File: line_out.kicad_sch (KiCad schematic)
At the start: 0 parts

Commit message: updates
* add line out
* fix almost all erc
* some more random edits
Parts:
- added C154, C157: 10u, invendelirium_audio:C_0603, symbol Device:C
- added C155: 1u, invendelirium_audio:C_0603, symbol Device:C
- added C156: 100n, invendelirium_audio:C_0603, symbol Device:C
- added C158, C159, C160, C161: 5.6n, invendelirium_audio:C_0603, symbol Device:C
- added D19, D20: 5V, symbol Device:D_TVS
- added J8: AudioJack4, Connector_Audio:Jack_3.5mm_PJ320D_Horizontal, symbol Connector_Audio:AudioJack4
- added R223, R233, R237, R238: 560, invendelirium_audio:R_0603, symbol Device:R_Small
- added R224, R225, R231, R232: 20k, invendelirium_audio:R_0603, symbol Device:R_Small
- added R226, R229: 560?, invendelirium_audio:R_0603, symbol Device:R_Small
- added R227, R236: 1k, invendelirium_audio:R_0603, symbol Device:R_Small
- added R228, R230, R234, R235: 4.7k, invendelirium_audio:R_0603, symbol Device:R_Small
- added R239: 10, invendelirium_audio:R_0603, symbol Device:R_Small
- added U29: max97220, invendelirium_audio:qfn_4p4p_3x3mm, symbol invendelirium_audio:max97220
- added s32: lineout0, invendelirium_general:pad_1.2x1.5, symbol Connector:TestPoint
- added s33: lineout1, invendelirium_general:pad_1.2x1.5, symbol Connector:TestPoint
- added s34: lineout2, invendelirium_general:pad_1.2x1.5, symbol Connector:TestPoint
- added s35: lineout3, invendelirium_general:pad_1.2x1.5, symbol Connector:TestPoint
- added s36: ref, invendelirium_general:pad_1.2x1.5, symbol Connector:TestPoint
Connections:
- new net: D20.2 (A2), J8.R1, R232.2, R236.2, U29.10, s33.1
- new net: D19.2 (A2), J8.T, R224.2, R227.2, U29.12, s32.1
- new net: R226.2, R235.1
- new net: C154.1, R239.2, U29.1 (pvdd), U29.13 (svdd), U29.9 (svdd2)
- new net: R230.2, R231.1, U29.7 (+)
- new net: C159.1, R223.2, R228.1
- new net: C158.1, R233.2, R234.1
- new net: R225.1, R235.2, U29.15 (+)
- new net: R228.2, R232.1, U29.8 (-)
- new net: C157.1, U29.5 (pvss)
- new net: C161.1, R238.2, s35.1
- new net: C160.1, R237.2, s34.1
- new net: C155.1, U29.4 (c1n)
- new net: C155.2, U29.2 (c1p)
- new net: R224.1, R234.2, U29.14 (-)
- new net: R229.2, R230.1
- new net: C156.1, U29.11 (bias)
- new net 5V: R239.1
- new net GND: C154.2, C156.2, C157.2, C158.2, C159.2, C160.2, C161.2, D19.1 (A1), D20.1 (A1), J8.R2, J8.S, R225.2, R227.1, R231.2, R236.1, U29.3 (pgnd), U29.6 (sgnd)
- new net en: U29.16 (EN)
- new net input_ref: R226.1, R229.1, s36.1
- new net s0: R233.1
- new net s1: R223.1
- new net s2: R237.1
- new net s3: R238.1
- no-connect marks 0 -> 1

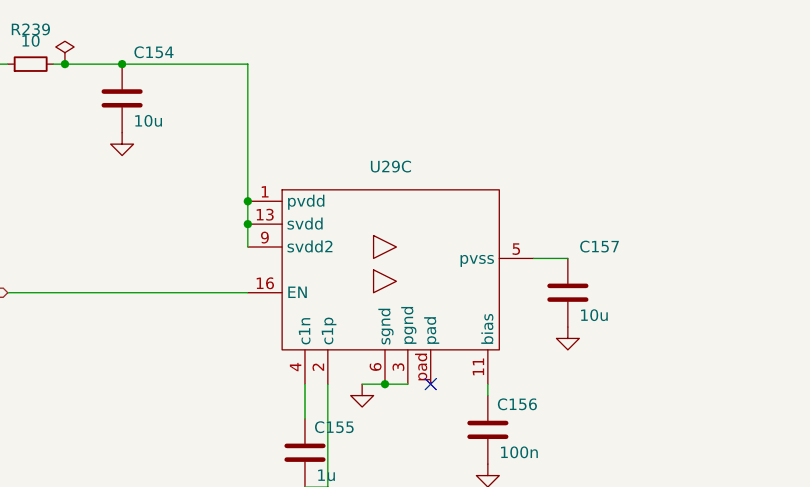
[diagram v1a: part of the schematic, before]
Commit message: add power input +...
+ tons of fixes, footprint assignments, etc
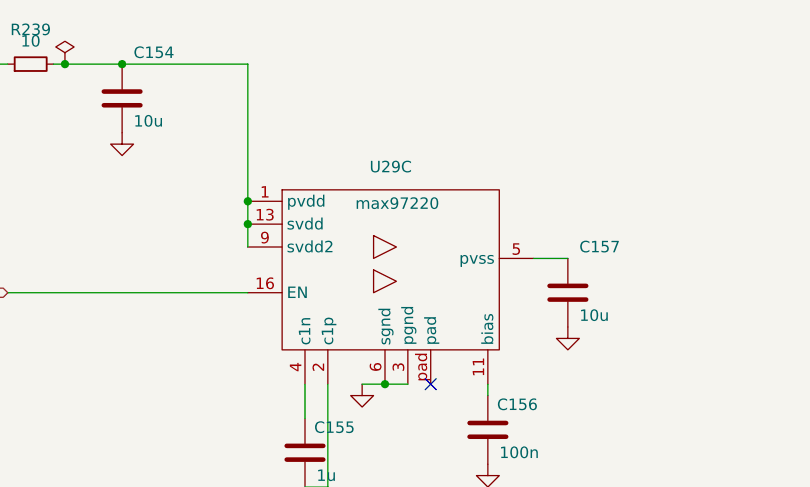
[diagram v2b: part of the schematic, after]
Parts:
- D19, D20: footprint (none) -> invendelirium_general:D_SOD-523_bidi

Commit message: routing routing...
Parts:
- added s41: -5V, invendelirium_general:pad_1.2x1.5, symbol Connector:TestPoint
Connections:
- net GND: now also U29.pad
- net lineout1: now reaches D20.2 (A2), J8.R1, R232.2, R236.2, U29.10
- net lineout1: no longer s33.1
- net lineout0: now reaches D19.2 (A2), J8.T, R224.2, R227.2, U29.12
- net lineout0: no longer s32.1
- net at C159.1, R223.2, R228.1: now also s33.1
- net at C158.1, R233.2, R234.1: now also s32.1
- net at C157.1, U29.5 (pvss): now also s41.1
- net lineout3: now reaches C161.1, R238.2, s35.1
- net lineout2: now reaches C160.1, R237.2, s34.1
- no-connect marks 1 -> 0
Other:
- moved on the sheet: s32, s33

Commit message: fill in some part numbers
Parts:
- s32, s33, s34, s35, s36, s41: now left out of the parts list
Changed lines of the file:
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@@
 		(unit 1)
 		(exclude_from_sim no)
-		(in_bom yes)
+		(in_bom no)
 		(on_board yes)
 		(dnp no)
@@
 		(unit 1)
 		(exclude_from_sim no)
-		(in_bom yes)
+		(in_bom no)
 		(on_board yes)
 		(dnp no)
@@
 		(unit 1)
 		(exclude_from_sim no)
-		(in_bom yes)
+		(in_bom no)
 		(on_board yes)
 		(dnp no)
@@
 		(unit 1)
 		(exclude_from_sim no)
-		(in_bom yes)
+		(in_bom no)
 		(on_board yes)
 		(dnp no)
@@
 		(unit 1)
 		(exclude_from_sim no)
-		(in_bom yes)
+		(in_bom no)
 		(on_board yes)
 		(dnp no)
@@
 		(unit 1)
 		(exclude_from_sim no)
-		(in_bom yes)
-		(on_board yes)
-		(dnp no)
+		(in_bom no)
+		(on_board yes)
+		(dnp no)

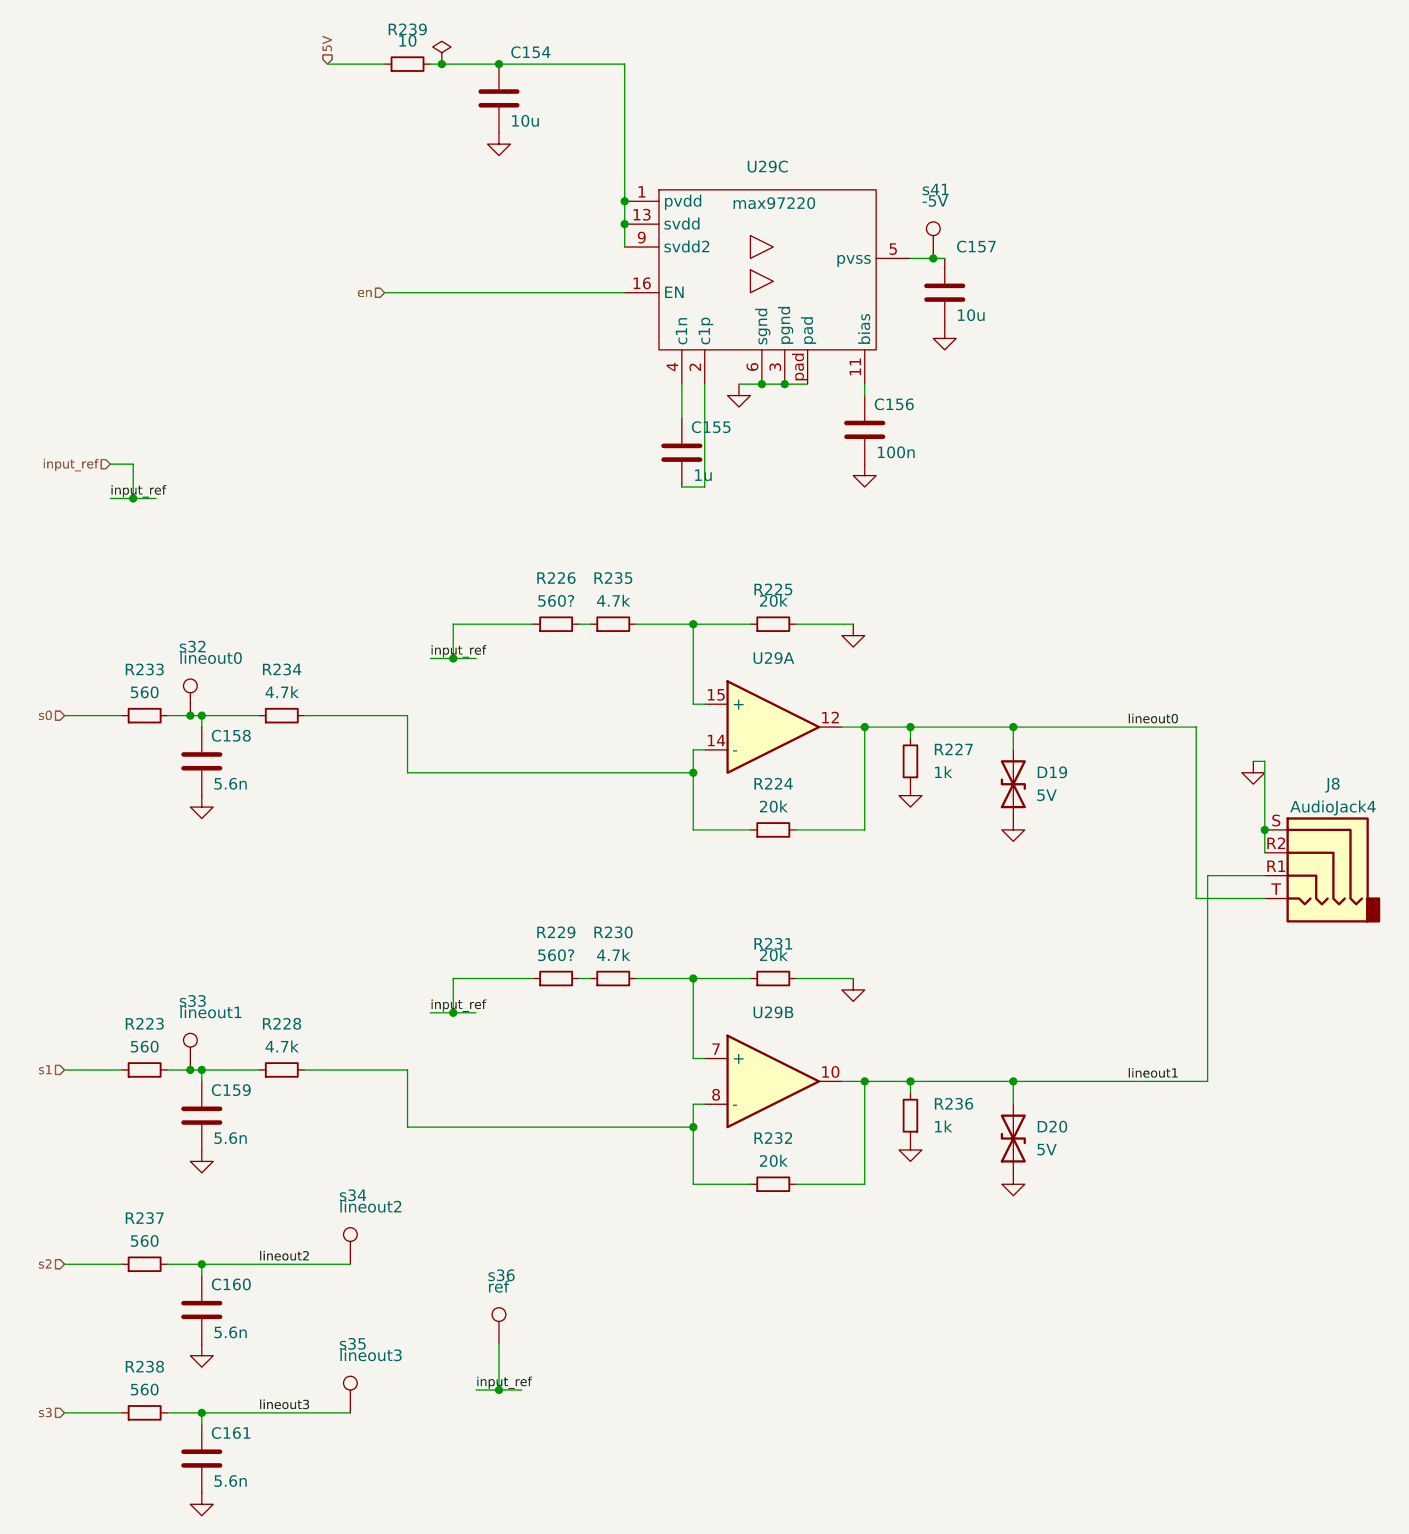
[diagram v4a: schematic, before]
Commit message: update values to what's being used + mark thin film resistors
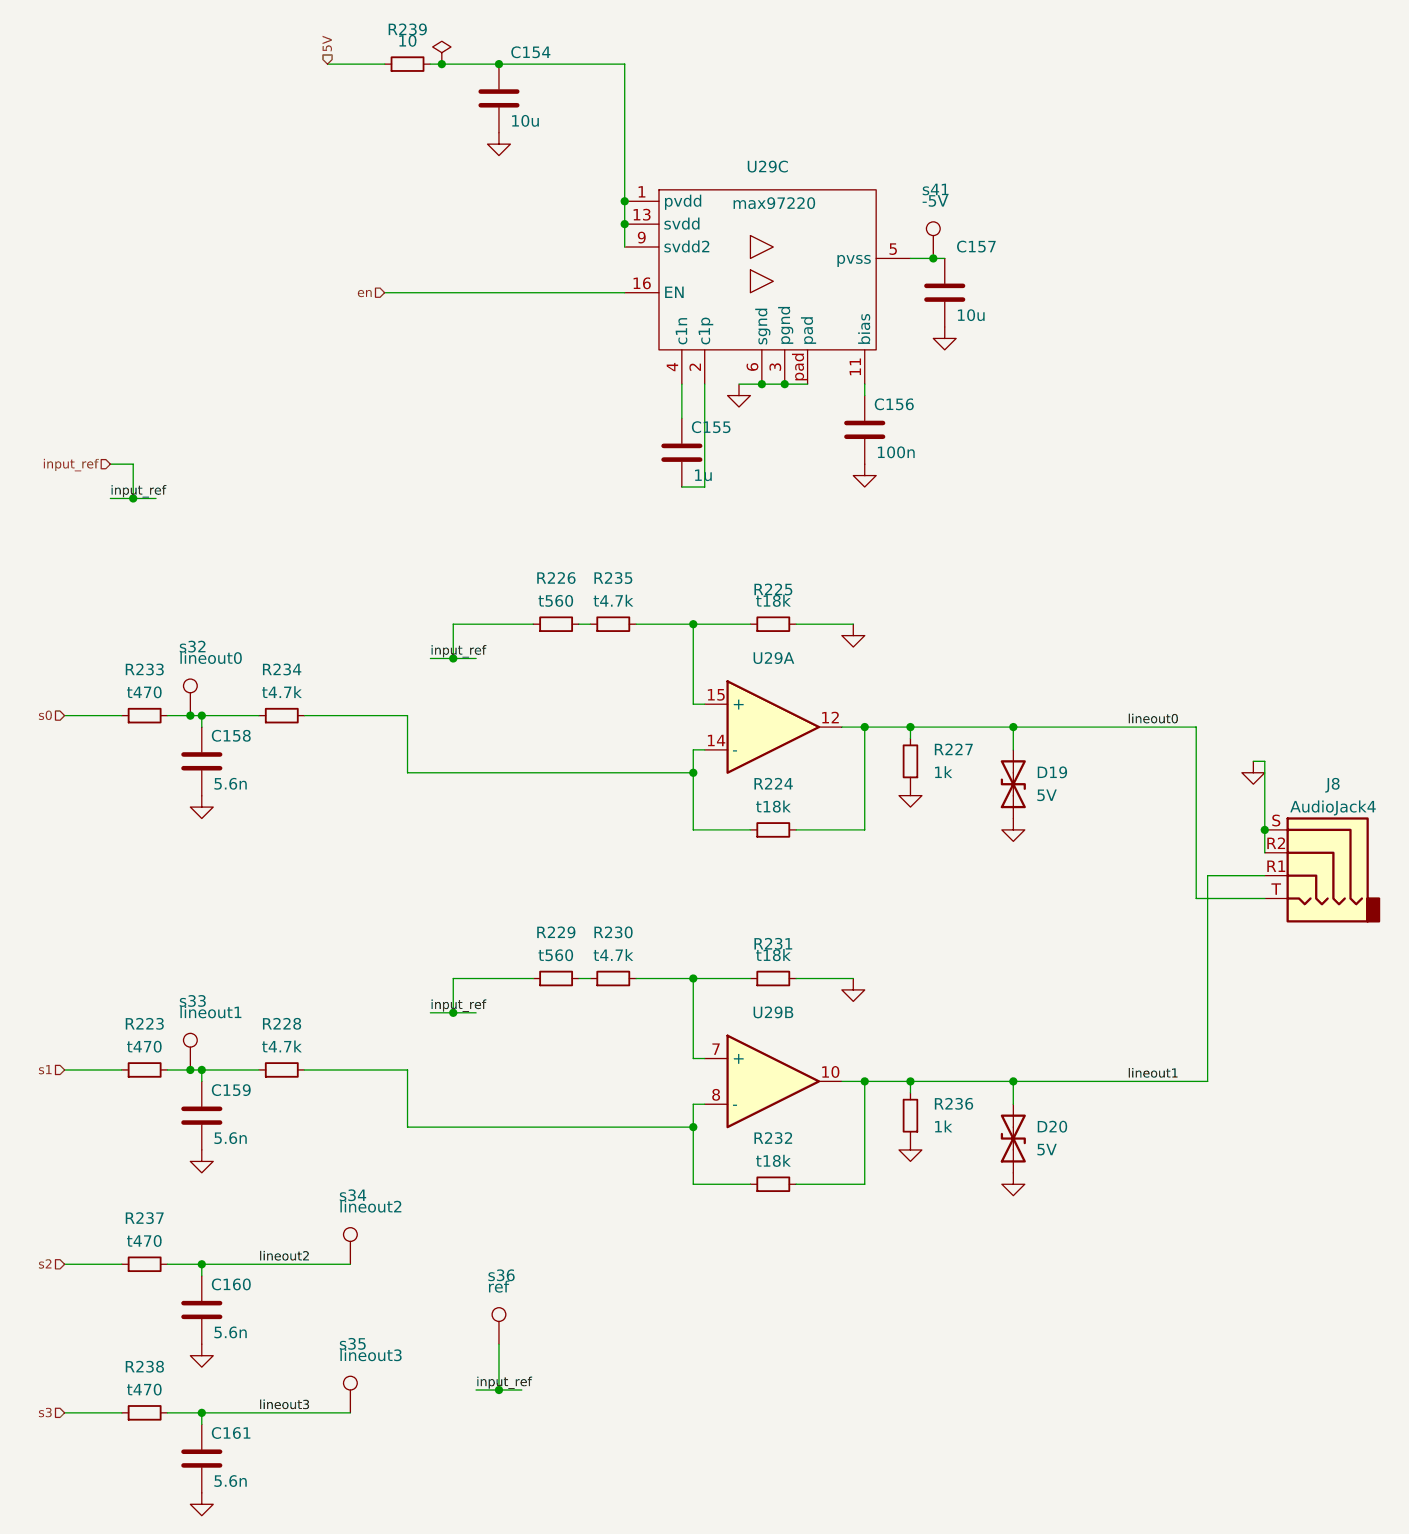
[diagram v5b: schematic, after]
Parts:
- R223, R233, R237, R238: value 560 -> t470
- R224, R225, R231, R232: value 20k -> t18k; PN (none) -> RT0603DRD0718KL
- R226, R229: value 560? -> t560
- R228, R230, R234, R235: value 4.7k -> t4.7k
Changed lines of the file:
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@@
 			)
 		)
-		(property "Value" "560?"
+		(property "Value" "t560"
 			(at 82.55 95.25 90)
 			(effects
@@
 			)
 		)
-		(property "Value" "20k"
+		(property "Value" "t18k"
 			(at 106.68 134.62 90)
 			(effects
@@
 			)
 		)
+		(property "PN" "RT0603DRD0718KL"
+			(at 106.68 137.16 0)
+			(effects
+				(font
+					(size 1.27 1.27)
+				)
+				(hide yes)
+			)
+		)
 		(pin "1"
 		)
@@
 			)
 		)
-		(property "Value" "560"
+		(property "Value" "t470"
 			(at 36.83 144.78 90)
 			(effects
@@
 			)
 		)
-		(property "Value" "4.7k"
+		(property "Value" "t4.7k"
 			(at 88.9 95.25 90)
 			(effects
@@
 			)
 		)
-		(property "Value" "560"
+		(property "Value" "t470"
 			(at 36.83 105.41 90)
 			(effects
@@
 			)
 		)
-		(property "Value" "20k"
+		(property "Value" "t18k"
 			(at 106.68 118.11 90)
 			(effects
@@
 			)
 		)
+		(property "PN" "RT0603DRD0718KL"
+			(at 106.68 120.65 0)
+			(effects
+				(font
+					(size 1.27 1.27)
+				)
+				(hide yes)
+			)
+		)
 		(pin "1"
 		)
@@
 			)
 		)
-		(property "Value" "560"
+		(property "Value" "t470"
 			(at 36.83 166.37 90)
 			(effects
@@
 			)
 		)
-		(property "Value" "560"
+		(property "Value" "t470"
 			(at 36.83 182.88 90)
 			(effects
@@
 			)
 		)
-		(property "Value" "20k"
+		(property "Value" "t18k"
 			(at 106.68 157.48 90)
 			(effects
@@
 			)
 		)
+		(property "PN" "RT0603DRD0718KL"
+			(at 106.68 160.02 0)
+			(effects
+				(font
+					(size 1.27 1.27)
+				)
+				(hide yes)
+			)
+		)
 		(pin "1"
 		)
@@
 			)
 		)
-		(property "Value" "4.7k"
+		(property "Value" "t4.7k"
 			(at 52.07 105.41 90)
 			(effects
@@
 			)
 		)
-		(property "Value" "4.7k"
+		(property "Value" "t4.7k"
 			(at 88.9 134.62 90)
 			(effects
@@
 			)
 		)
-		(property "Value" "560?"
+		(property "Value" "t560"
 			(at 82.55 134.62 90)
 			(effects
@@
 			)
 		)
-		(property "Value" "4.7k"
+		(property "Value" "t4.7k"
 			(at 52.07 144.78 90)
 			(effects
@@
 			)
 		)
-		(property "Value" "20k"
+		(property "Value" "t18k"
 			(at 106.68 95.25 90)
 			(effects
@@
 			(at 106.68 97.79 0)
 			(effects
+				(font
+					(size 1.27 1.27)
+				)
+				(hide yes)
+			)
+		)
+		(property "PN" "RT0603DRD0718KL"
+			(at 106.68 97.79 0)
+			(effects

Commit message: work on bugs
* align parts
* enlarge cercaps
* fix ak caps
* improve jack footprint
* fix lmr stencil openings
* remove one ldo
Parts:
- C154, C157: footprint invendelirium_audio:C_0603 -> invendelirium_audio:C_0603_larger
- J8: footprint Connector_Audio:Jack_3.5mm_PJ320D_Horizontal -> invendelirium_audio:Jack_3.5mm_PJ320D_Horizontal
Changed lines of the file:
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@@
 			)
 		)
-		(property "Footprint" "Connector_Audio:Jack_3.5mm_PJ320D_Horizontal"
+		(property "Footprint" "invendelirium_audio:Jack_3.5mm_PJ320D_Horizontal"
 			(at 166.37 123.19 0)
 			(effects
@@
 			)
 		)
-		(property "Footprint" "invendelirium_audio:C_0603"
+		(property "Footprint" "invendelirium_audio:C_0603_larger"
 			(at 77.1652 43.18 0)
 			(effects
@@
 			)
 		)
-		(property "Footprint" "invendelirium_audio:C_0603"
+		(property "Footprint" "invendelirium_audio:C_0603_larger"
 			(at 126.6952 64.77 0)
 			(effects

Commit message: all known bugs fixed
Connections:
- net -5V: now reaches C157.1, U29.5 (pvss), s41.1
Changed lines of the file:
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@@
+	)
+	(junction
+		(at 125.73 57.15)
+		(diameter 0)
+		(color 0 0 0 0)
 	)
 	(junction
@@
 		(pts
 			(xy 90.17 53.34) (xy 90.17 50.8)
+		)
+		(stroke
+			(width 0)
+			(type default)
+		)
+	)
+	(wire
+		(pts
+			(xy 125.73 57.15) (xy 138.43 57.15)
 		)
 		(stroke
@@
 		)
 	)
+	(hierarchical_label "-5V"
+		(shape output)
+		(at 138.43 57.15 0)
+		(fields_autoplaced yes)
+		(effects
+			(font
+				(size 1.016 1.016)
+			)
+			(justify left)
+		)
+	)
